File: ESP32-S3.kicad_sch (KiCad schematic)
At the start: 1 part, among them U1 ESP32-S3-DevKitC

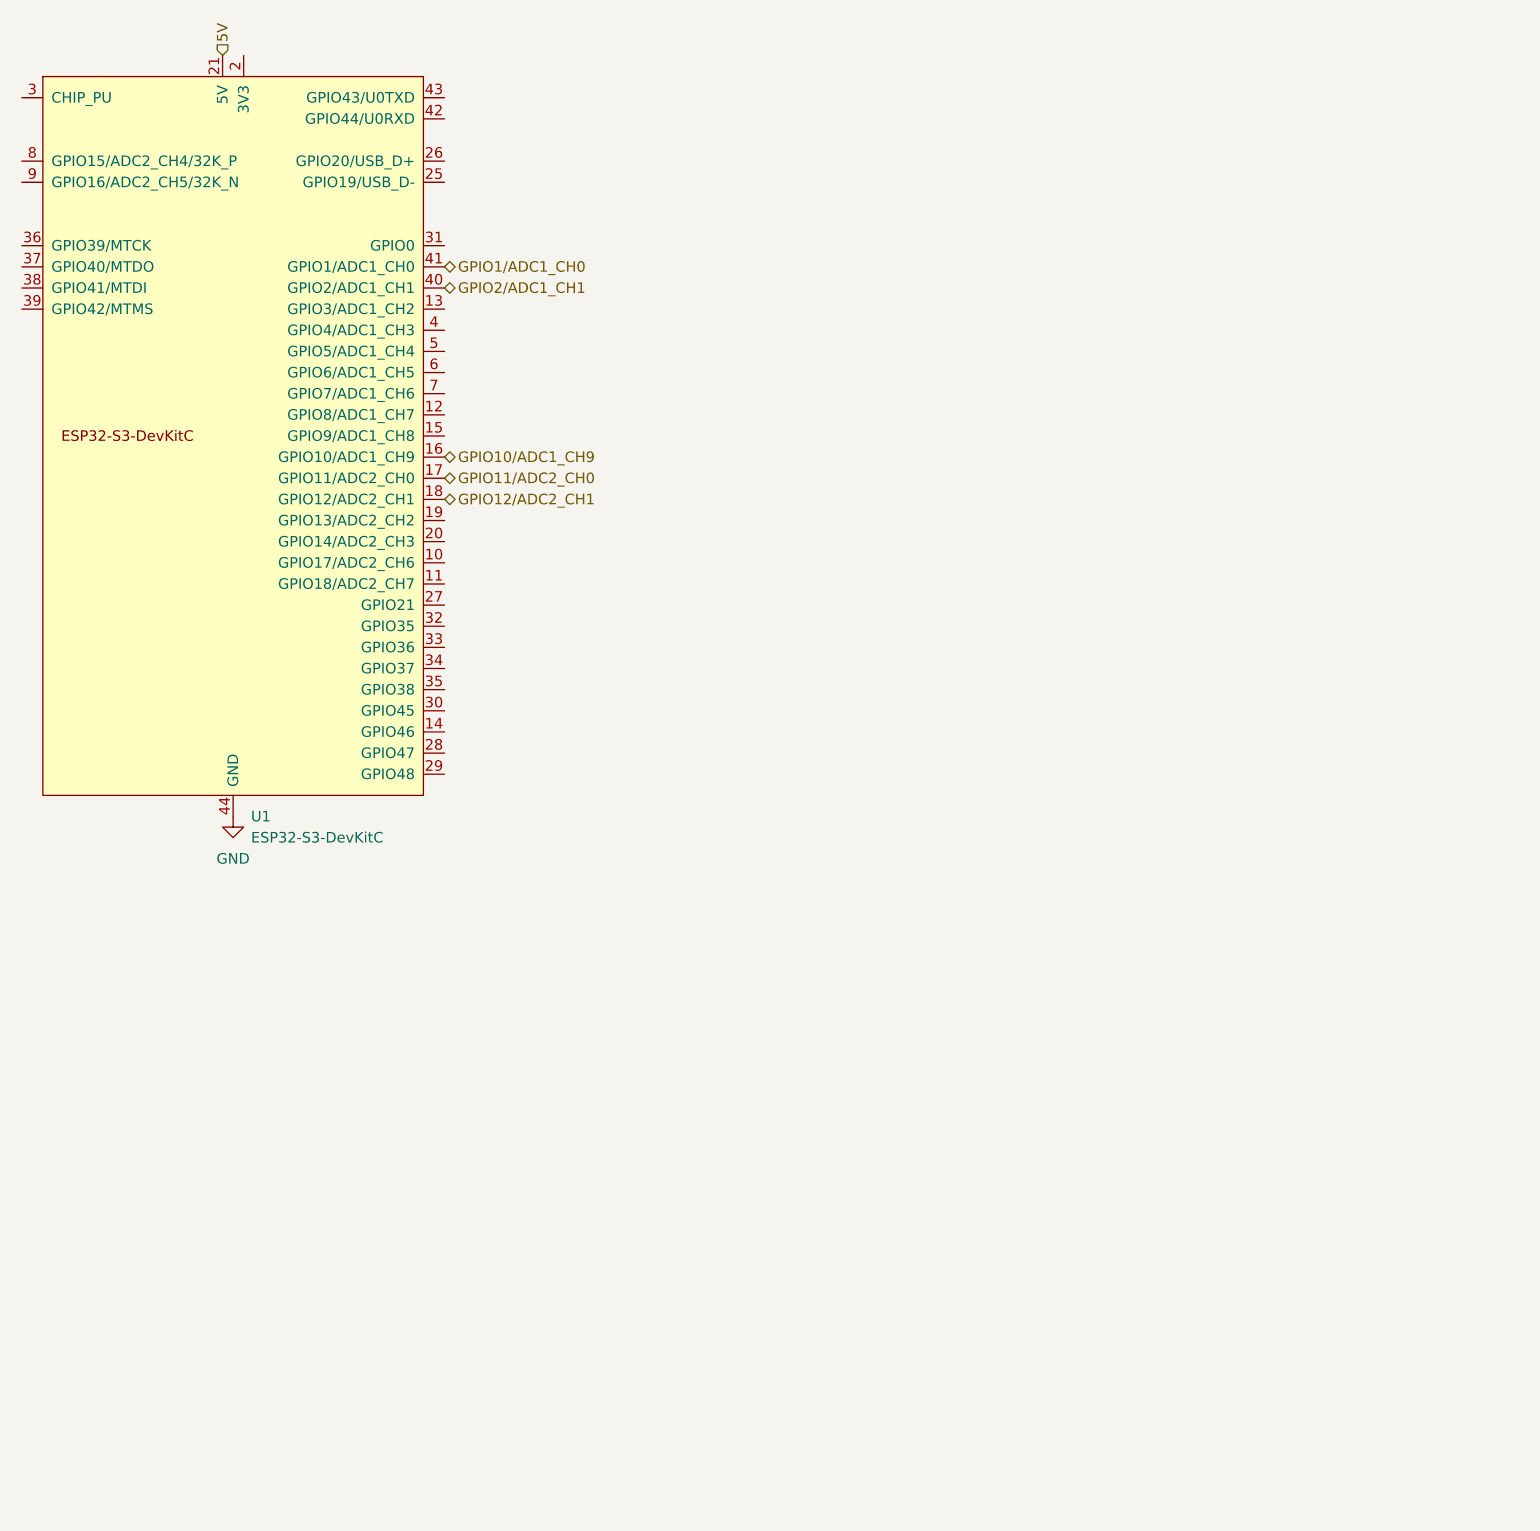
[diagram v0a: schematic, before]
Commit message: Update schematics: signal conditioning, power, ESP32-S3, output, and add signal measurement sub-sheet
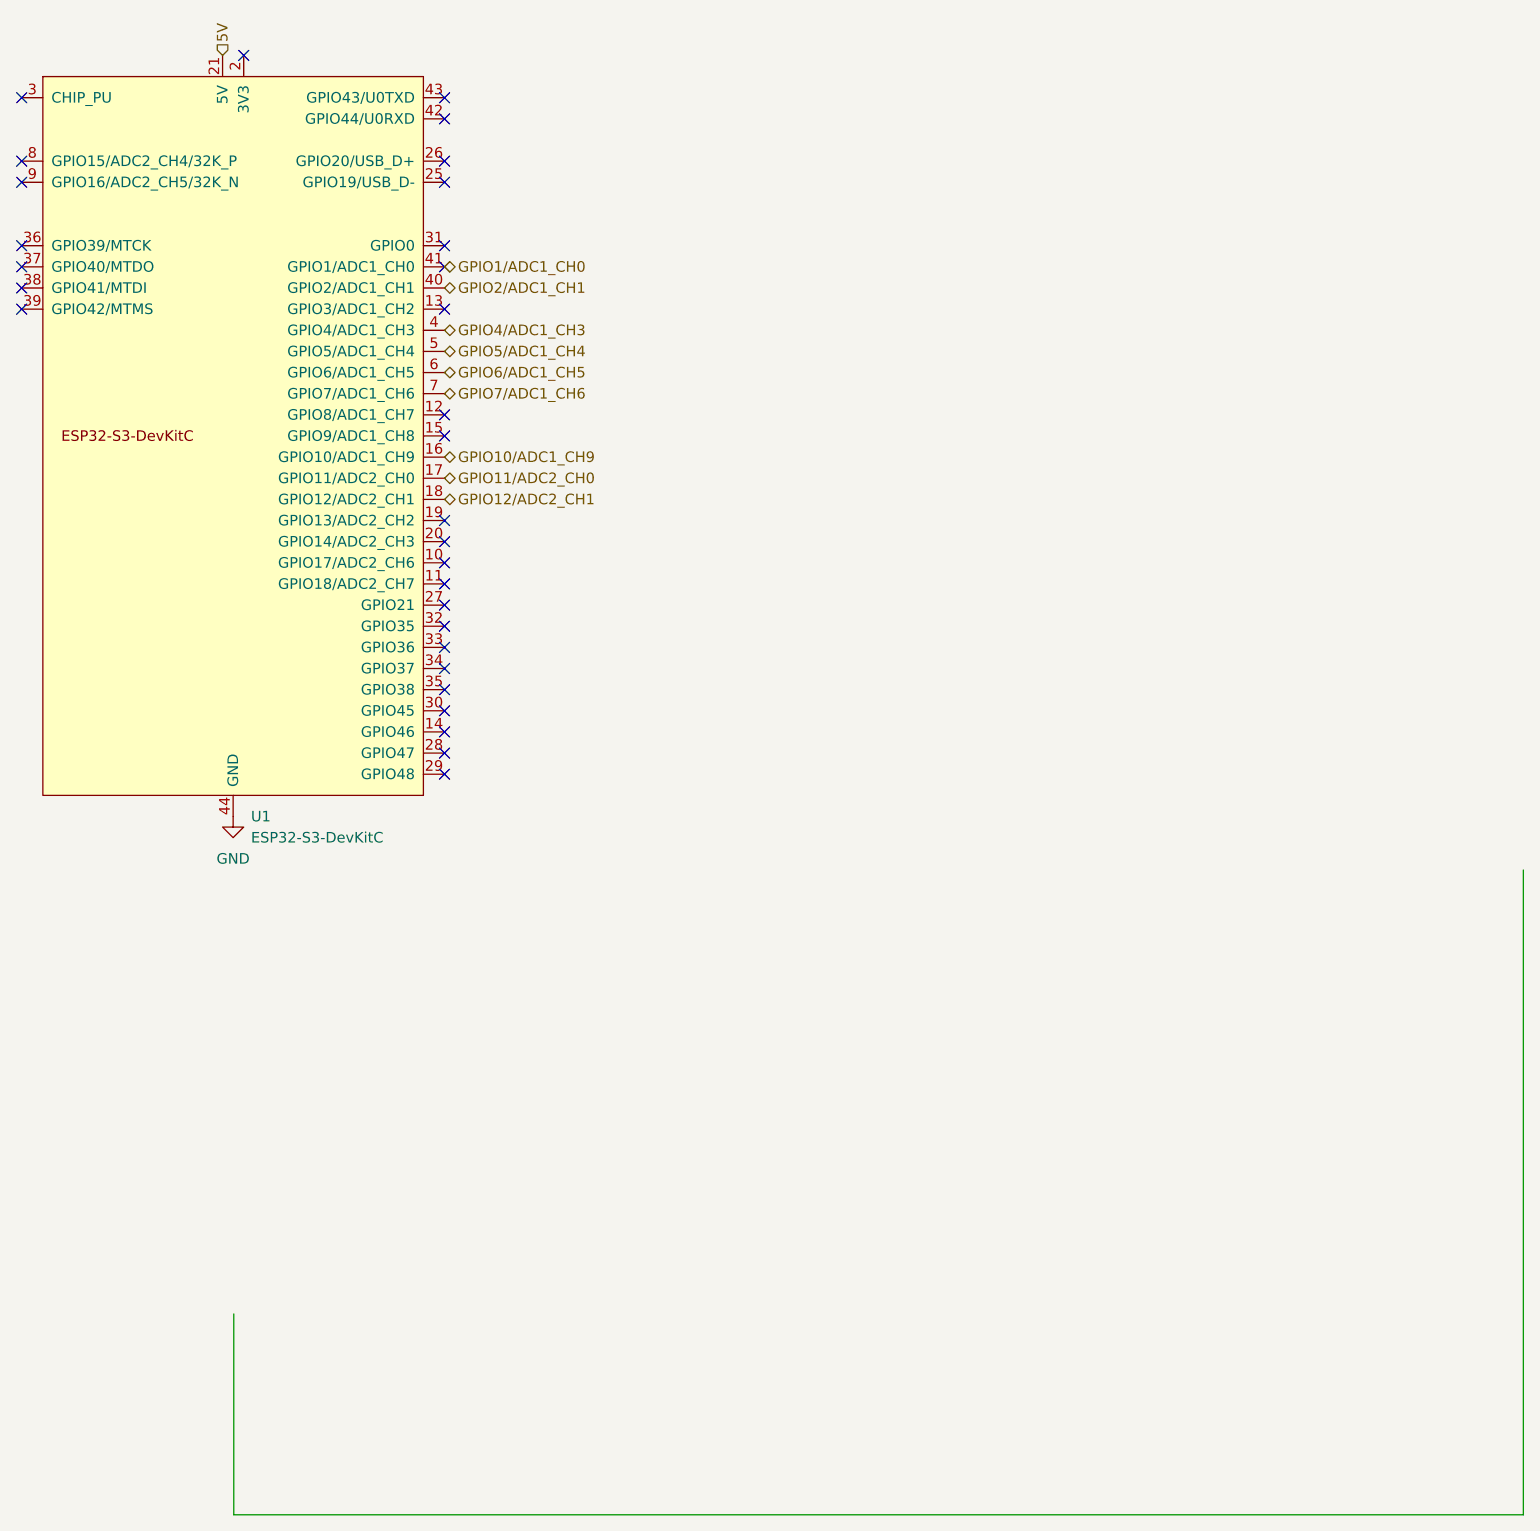
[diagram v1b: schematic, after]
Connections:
- net GPIO4/ADC1_CH3: now reaches U1.4 (GPIO4/ADC1_CH3)
- net GPIO5/ADC1_CH4: now reaches U1.5 (GPIO5/ADC1_CH4)
- net GPIO6/ADC1_CH5: now reaches U1.6 (GPIO6/ADC1_CH5)
- net GPIO7/ADC1_CH6: now reaches U1.7 (GPIO7/ADC1_CH6)
- no-connect marks 0 -> 30
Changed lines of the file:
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@@
 		(comment 1 "Aguilera Gabriel")
+	)
+	(no_connect
+		(at 168.91 124.46)
+	)
+	(no_connect
+		(at 168.91 76.2)
+	)
+	(no_connect
+		(at 118.11 50.8)
+	)
+	(no_connect
+		(at 144.78 45.72)
+	)
+	(no_connect
+		(at 168.91 104.14)
+	)
+	(no_connect
+		(at 168.91 116.84)
+	)
+	(no_connect
+		(at 168.91 60.96)
+	)
+	(no_connect
+		(at 168.91 132.08)
+	)
+	(no_connect
+		(at 168.91 111.76)
+	)
+	(no_connect
+		(at 168.91 91.44)
+	)
+	(no_connect
+		(at 118.11 73.66)
+	)
+	(no_connect
+		(at 168.91 106.68)
+	)
+	(no_connect
+		(at 118.11 58.42)
+	)
+	(no_connect
+		(at 118.11 68.58)
+	)
+	(no_connect
+		(at 168.91 109.22)
+	)
+	(no_connect
+		(at 168.91 119.38)
+	)
+	(no_connect
+		(at 168.91 53.34)
+	)
+	(no_connect
+		(at 168.91 101.6)
+	)
+	(no_connect
+		(at 168.91 129.54)
+	)
+	(no_connect
+		(at 168.91 68.58)
+	)
+	(no_connect
+		(at 168.91 50.8)
+	)
+	(no_connect
+		(at 168.91 71.12)
+	)
+	(no_connect
+		(at 118.11 60.96)
+	)
+	(no_connect
+		(at 168.91 127)
+	)
+	(no_connect
+		(at 168.91 58.42)
+	)
+	(no_connect
+		(at 168.91 88.9)
+	)
+	(no_connect
+		(at 118.11 71.12)
+	)
+	(no_connect
+		(at 168.91 114.3)
+	)
+	(no_connect
+		(at 168.91 121.92)
+	)
+	(no_connect
+		(at 118.11 76.2)
+	)
+	(wire
+		(pts
+			(xy 143.5862 221.0562) (xy 298.5262 221.0562)
+		)
+		(stroke
+			(width 0)
+			(type default)
+		)
+	)
+	(wire
+		(pts
+			(xy 298.5262 221.0562) (xy 298.5262 143.5862)
+		)
+		(stroke
+			(width 0)
+			(type default)
+		)
+	)
+	(wire
+		(pts
+			(xy 143.5862 196.9262) (xy 143.5862 221.0562)
+		)
+		(stroke
+			(width 0)
+			(type default)
+		)
+	)
+	(hierarchical_label "GPIO5/ADC1_CH4"
+		(shape bidirectional)
+		(at 168.91 81.28 0)
+		(effects
+			(font
+				(size 1.27 1.27)
+			)
+			(justify left)
+		)
 	)
 	(hierarchical_label "5V"
@@
 		)
 	)
+	(hierarchical_label "GPIO4/ADC1_CH3"
+		(shape bidirectional)
+		(at 168.91 78.74 0)
+		(effects
+			(font
+				(size 1.27 1.27)
+			)
+			(justify left)
+		)
+	)
+	(hierarchical_label "GPIO7/ADC1_CH6"
+		(shape bidirectional)
+		(at 168.91 86.36 0)
+		(effects
+			(font
+				(size 1.27 1.27)
+			)
+			(justify left)
+		)
+	)
 	(hierarchical_label "GPIO1/ADC1_CH0"
 		(shape bidirectional)
@@
 		(effects
 			(font
+				(size 1.27 1.27)
+			)
+			(justify left)
+		)
+	)
+	(hierarchical_label "GPIO6/ADC1_CH5"
+		(shape bidirectional)
+		(at 168.91 83.82 0)
+		(effects
+			(font
